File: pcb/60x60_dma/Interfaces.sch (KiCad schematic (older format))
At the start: 16 parts, among them J1 Conn_01x05, J10 Conn_01x01_Female, J11 Conn_01x01_Female, J12 Conn_01x01_Female, J13 Conn_01x01_Female, J14 Conn_01x02, J15 Conn_01x04, J2 Conn_01x05, J3 USB_OTG, J4 Conn_01x05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

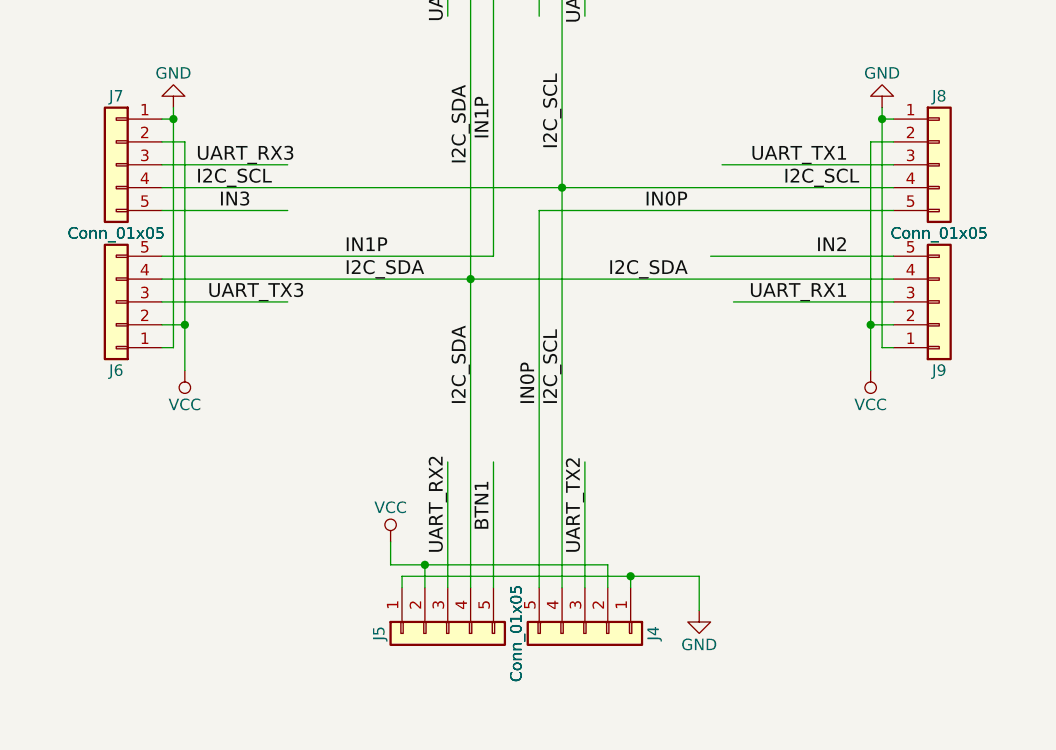
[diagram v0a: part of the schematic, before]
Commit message: - add 60x60_dma version
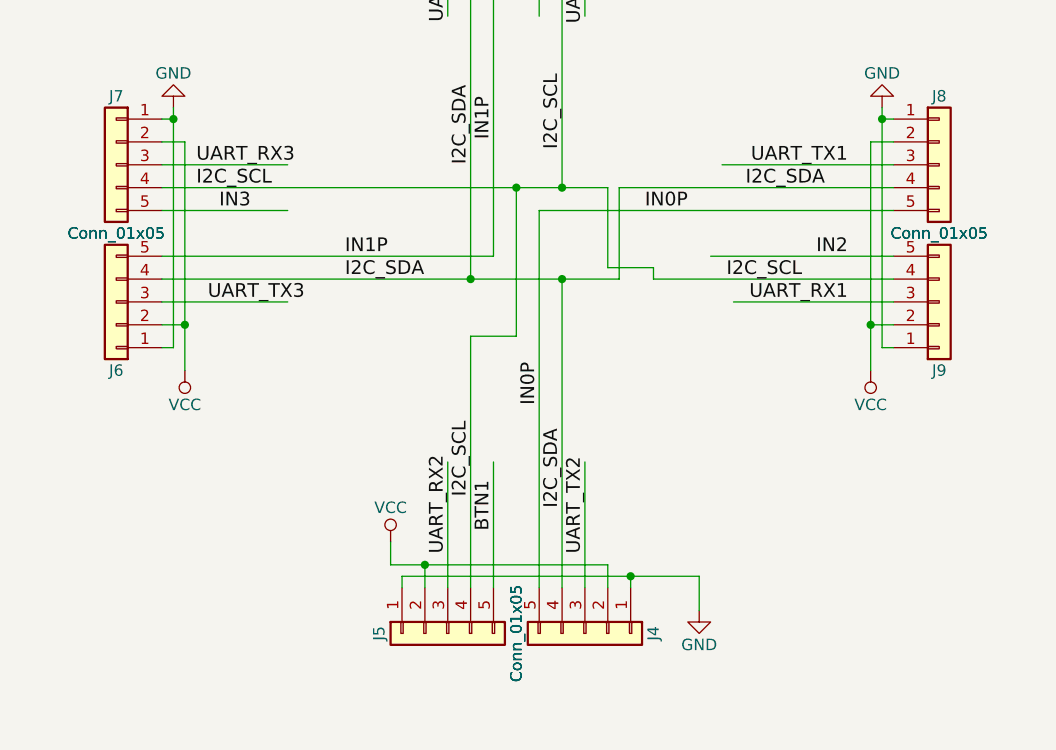
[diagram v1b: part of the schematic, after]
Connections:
- wire segments 96 -> 106
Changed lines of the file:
@@
 	-1   0    0    -1
 $EndComp
-Text Label 3950 4350 1    60   ~ 0
+Text Label 3550 4750 1    60   ~ 0
 I2C_SCL
 $Comp
@@
 	1    0    0    -1
 $EndComp
-Text Label 3550 4350 1    60   ~ 0
+Text Label 3950 4800 1    60   ~ 0
 I2C_SDA
 Text Label 4050 5000 1    60   ~ 0
@@
 Text Label 5200 3900 2    60   ~ 0
 UART_RX1
-Text Label 5250 3400 2    60   ~ 0
+Text Label 5000 3800 2    60   ~ 0
 I2C_SCL
 $Comp
@@
 	-1   0    0    1
 $EndComp
-Text Label 4500 3800 2    60   ~ 0
+Text Label 5100 3400 2    60   ~ 0
 I2C_SDA
 Text Label 2350 3300 0    60   ~ 0
@@
 	2200 3800 3550 3800
 Wire Wire Line
-	2200 3400 3950 3400
+	2200 3400 3750 3400
 Wire Wire Line
 	9450 3900 9850 3900
@@
 	9300 2300 9300 2350
 Wire Wire Line
-	3950 3400 3950 5150
-Wire Wire Line
-	3950 3400 5400 3400
-Wire Wire Line
-	3550 3800 3550 5150
-Wire Wire Line
-	3550 3800 5400 3800
+	5400 3400 4200 3400
+Wire Wire Line
+	4200 3400 4200 3800
+Wire Wire Line
+	4200 3800 3950 3800
+Wire Wire Line
+	3950 3400 4150 3400
+Wire Wire Line
+	4150 3400 4150 3750
+Wire Wire Line
+	4150 3750 4350 3750
+Wire Wire Line
+	4350 3750 4350 3800
+Wire Wire Line
+	4350 3800 5400 3800
+Wire Wire Line
+	3950 3800 3950 5150
+Connection ~ 3950 3800
+Wire Wire Line
+	3950 3800 3550 3800
+Wire Wire Line
+	3550 5150 3550 4050
+Wire Wire Line
+	3550 4050 3750 4050
+Wire Wire Line
+	3750 4050 3750 3400
+Connection ~ 3750 3400
+Wire Wire Line
+	3750 3400 3950 3400
 $EndSCHEMATC

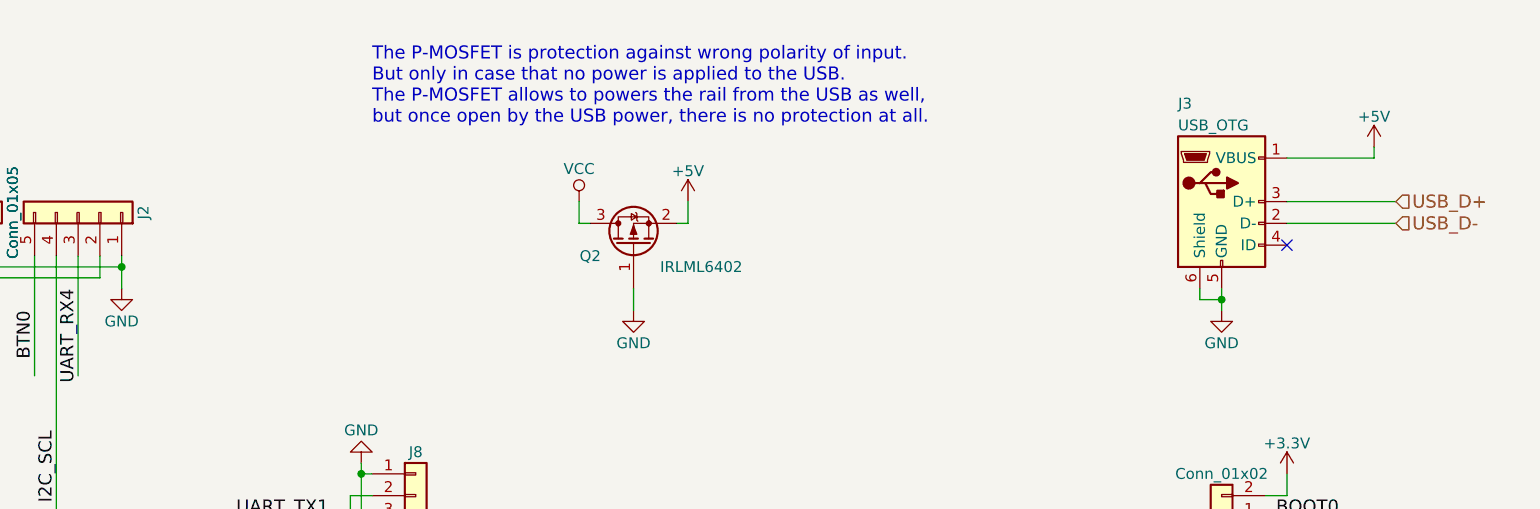
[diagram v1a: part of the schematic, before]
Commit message: - add some testpoints
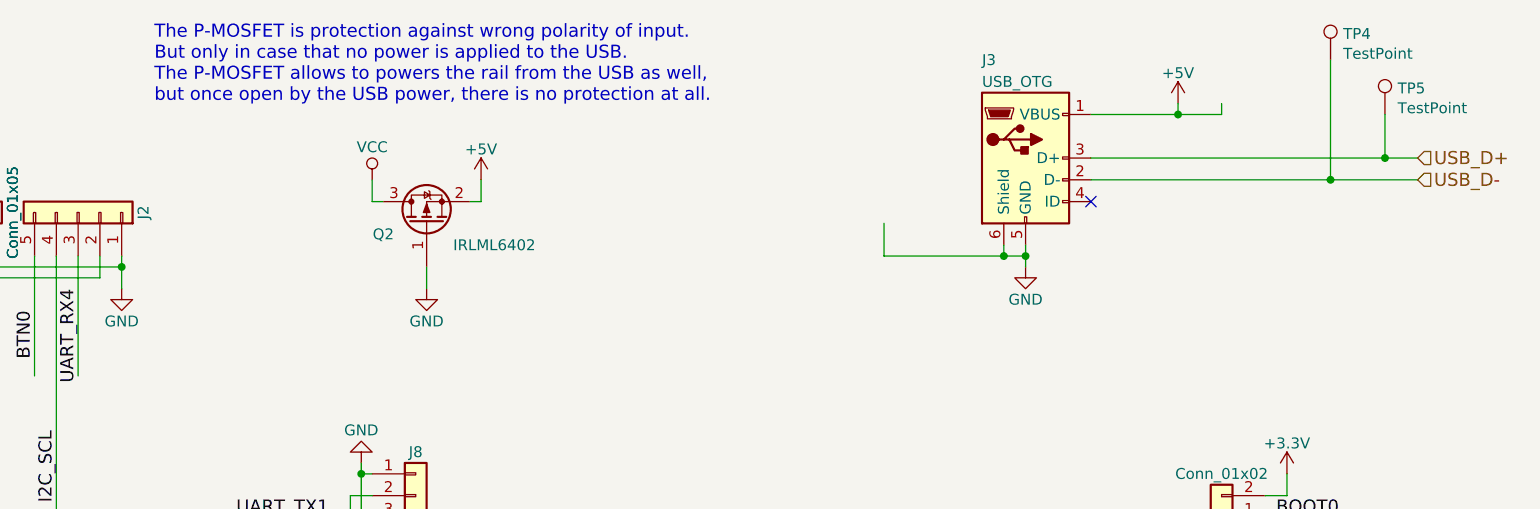
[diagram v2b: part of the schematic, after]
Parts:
- added TP4, TP5: TestPoint, symbol Connector:TestPoint
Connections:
- wire segments 106 -> 114
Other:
- moved on the sheet: J3, Q2
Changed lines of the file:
@@
 L bcl4v2-rescue:USB_OTG J3
 U 1 1 5BD73B46
-P 9300 1850
-F 0 "J3" H 9100 2300 50  0000 L CNN
-F 1 "USB_OTG" H 9100 2200 50  0000 L CNN
-F 2 "Connect:USB_Micro-B" H 9450 1800 50  0001 C CNN
-F 3 "" H 9450 1800 50  0001 C CNN
-	1    9300 1850
-	1    0    0    -1
-$EndComp
-NoConn ~ 9600 2050
+P 8400 1650
+F 0 "J3" H 8200 2100 50  0000 L CNN
+F 1 "USB_OTG" H 8200 2000 50  0000 L CNN
+F 2 "Connect:USB_Micro-B" H 8550 1600 50  0001 C CNN
+F 3 "" H 8550 1600 50  0001 C CNN
+	1    8400 1650
+	1    0    0    -1
+$EndComp
+NoConn ~ 8700 1850
 $Comp
 L bcl4v2-rescue:+5V #PWR039
 U 1 1 5BD73B57
-P 10000 1600
-F 0 "#PWR039" H 10000 1450 50  0001 C CNN
-F 1 "+5V" H 10000 1740 50  0000 C CNN
-F 2 "" H 10000 1600 50  0001 C CNN
-F 3 "" H 10000 1600 50  0001 C CNN
-	1    10000 1600
+P 9100 1400
+F 0 "#PWR039" H 9100 1250 50  0001 C CNN
+F 1 "+5V" H 9100 1540 50  0000 C CNN
+F 2 "" H 9100 1400 50  0001 C CNN
+F 3 "" H 9100 1400 50  0001 C CNN
+	1    9100 1400
 	1    0    0    -1
 $EndComp
@@
 L bcl4v2-rescue:GND #PWR042
 U 1 1 5BD73B89
-P 9300 2350
-F 0 "#PWR042" H 9300 2100 50  0001 C CNN
-F 1 "GND" H 9300 2200 50  0000 C CNN
-F 2 "" H 9300 2350 50  0001 C CNN
-F 3 "" H 9300 2350 50  0001 C CNN
-	1    9300 2350
+P 8400 2150
+F 0 "#PWR042" H 8400 1900 50  0001 C CNN
+F 1 "GND" H 8400 2000 50  0000 C CNN
+F 2 "" H 8400 2150 50  0001 C CNN
+F 3 "" H 8400 2150 50  0001 C CNN
+	1    8400 2150
 	1    0    0    -1
 $EndComp
@@
 Text HLabel 5400 6200 0    60   Input ~ 0
 I2C_SCL
-Text HLabel 10100 1950 2    60   Input ~ 0
+Text HLabel 10200 1750 2    60   Input ~ 0
 USB_D-
-Text HLabel 10100 1850 2    60   Input ~ 0
+Text HLabel 10200 1650 2    60   Input ~ 0
 USB_D+
 Text HLabel 3700 6150 0    60   Input ~ 0
@@
 L bcl4v2-rescue:+5V #PWR043
 U 1 1 5BDD7179
-P 6850 1850
-F 0 "#PWR043" H 6850 1700 50  0001 C CNN
-F 1 "+5V" H 6850 1990 50  0000 C CNN
-F 2 "" H 6850 1850 50  0001 C CNN
-F 3 "" H 6850 1850 50  0001 C CNN
-	1    6850 1850
+P 5900 1750
+F 0 "#PWR043" H 5900 1600 50  0001 C CNN
+F 1 "+5V" H 5900 1890 50  0000 C CNN
+F 2 "" H 5900 1750 50  0001 C CNN
+F 3 "" H 5900 1750 50  0001 C CNN
+	1    5900 1750
 	1    0    0    -1
 $EndComp
@@
 L bcl4v2-rescue:VCC #PWR044
 U 1 1 5BDD717F
-P 6350 1850
-F 0 "#PWR044" H 6350 1700 50  0001 C CNN
-F 1 "VCC" H 6350 2000 50  0000 C CNN
-F 2 "" H 6350 1850 50  0001 C CNN
-F 3 "" H 6350 1850 50  0001 C CNN
-	1    6350 1850
+P 5400 1750
+F 0 "#PWR044" H 5400 1600 50  0001 C CNN
+F 1 "VCC" H 5400 1900 50  0000 C CNN
+F 2 "" H 5400 1750 50  0001 C CNN
+F 3 "" H 5400 1750 50  0001 C CNN
+	1    5400 1750
 	1    0    0    -1
 $EndComp
@@
 L bcl4v2-rescue:Q_PMOS_GSD Q2
 U 1 1 5BDD7457
-P 6600 2050
-F 0 "Q2" V 6550 2200 50  0000 L CNN
-F 1 "IRLML6402" V 6500 1550 50  0000 L CNN
-F 2 "kicad_libraries_new:badger_SOT-23_handsolder" H 6800 2150 50  0001 C CNN
-F 3 "" H 6600 2050 50  0001 C CNN
-	1    6600 2050
+P 5650 1950
+F 0 "Q2" V 5600 2100 50  0000 L CNN
+F 1 "IRLML6402" V 5550 1450 50  0000 L CNN
+F 2 "kicad_libraries_new:badger_SOT-23_handsolder" H 5850 2050 50  0001 C CNN
+F 3 "" H 5650 1950 50  0001 C CNN
+	1    5650 1950
 	0    -1   -1   0
 $EndComp
@@
 L bcl4v2-rescue:GND #PWR045
 U 1 1 5BDD7A19
-P 6600 2350
-F 0 "#PWR045" H 6600 2100 50  0001 C CNN
-F 1 "GND" H 6600 2200 50  0000 C CNN
-F 2 "" H 6600 2350 50  0001 C CNN
-F 3 "" H 6600 2350 50  0001 C CNN
-	1    6600 2350
-	1    0    0    -1
-$EndComp
-Text Notes 5400 1500 0    60   ~ 0
+P 5650 2250
+F 0 "#PWR045" H 5650 2000 50  0001 C CNN
+F 1 "GND" H 5650 2100 50  0000 C CNN
+F 2 "" H 5650 2250 50  0001 C CNN
+F 3 "" H 5650 2250 50  0001 C CNN
+	1    5650 2250
+	1    0    0    -1
+$EndComp
+Text Notes 4400 1400 0    60   ~ 0
 The P-MOSFET is protection against wrong polarity of input.\nBut only in case that no power is applied to the USB.\nThe P-MOSFET allows to powers the rail from the USB as well,\nbut once open by the USB power, there is no protection at all.
 Text Label 1650 6850 0    60   ~ 0
@@
 	9450 3800 9850 3800
 Wire Wire Line
-	9200 2250 9200 2300
-Wire Wire Line
-	9200 2300 9300 2300
-Wire Wire Line
-	9300 2250 9300 2300
-Connection ~ 9300 2300
-Wire Wire Line
-	9600 1850 10100 1850
-Wire Wire Line
-	9600 1950 10100 1950
-Wire Wire Line
-	9600 1650 10000 1650
-Wire Wire Line
-	10000 1650 10000 1600
+	8300 2050 8300 2100
+Wire Wire Line
+	8300 2100 8400 2100
+Wire Wire Line
+	8400 2050 8400 2100
+Connection ~ 8400 2100
+Wire Wire Line
+	8700 1450 9100 1450
+Wire Wire Line
+	9100 1450 9100 1400
 Wire Wire Line
 	9500 3300 9850 3300
@@
 	9600 3200 9600 3100
 Wire Wire Line
-	6600 2250 6600 2350
-Wire Wire Line
-	6850 1950 6800 1950
-Wire Wire Line
-	6350 1950 6400 1950
-Wire Wire Line
-	6850 1850 6850 1950
-Wire Wire Line
-	6350 1850 6350 1950
+	5650 2150 5650 2250
+Wire Wire Line
+	5900 1850 5850 1850
+Wire Wire Line
+	5400 1850 5450 1850
+Wire Wire Line
+	5900 1750 5900 1850
+Wire Wire Line
+	5400 1750 5400 1850
 Wire Wire Line
 	1600 6100 2100 6100
@@
 	2300 4000 2300 3200
 Wire Wire Line
-	9300 2300 9300 2350
+	8400 2100 8400 2150
 Wire Wire Line
 	5400 3400 4200 3400
@@
 Wire Wire Line
 	3750 3400 3950 3400
+$Comp
+L Connector:TestPoint TP4
+U 1 1 5C7F78D4
+P 9800 1200
+F 0 "TP4" H 9858 1320 50  0000 L CNN
+F 1 "TestPoint" H 9858 1229 50  0000 L CNN
+F 2 "" H 10000 1200 50  0001 C CNN
+F 3 "~" H 10000 1200 50  0001 C CNN
+	1    9800 1200
+	1    0    0    -1
+$EndComp
+Wire Wire Line
+	8300 2100 7750 2100
+Wire Wire Line
+	7750 2100 7750 1950
+Connection ~ 8300 2100
+Wire Wire Line
+	9300 1400 9300 1450
+Wire Wire Line
+	9300 1450 9100 1450
+Connection ~ 9100 1450
+Wire Wire Line
+	8700 1650 10050 1650
+Wire Wire Line
+	8700 1750 9800 1750
+Wire Wire Line
+	9800 1200 9800 1750
+Connection ~ 9800 1750
+Wire Wire Line
+	9800 1750 10200 1750
+Wire Wire Line
+	10050 1450 10050 1650
+Connection ~ 10050 1650
+Wire Wire Line
+	10050 1650 10200 1650
+$Comp
+L Connector:TestPoint TP5
+U 1 1 5C7F782D
+P 10050 1450
+F 0 "TP5" H 10108 1570 50  0000 L CNN
+F 1 "TestPoint" H 10108 1479 50  0000 L CNN
+F 2 "" H 10250 1450 50  0001 C CNN
+F 3 "~" H 10250 1450 50  0001 C CNN
+	1    10050 1450
+	1    0    0    -1
+$EndComp
 $EndSCHEMATC

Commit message: - fix display connections, add testpoints
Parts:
- TP4, TP5: footprint (none) -> TestPoint:TestPoint_Pad_D1.0mm
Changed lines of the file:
@@
 F 0 "TP4" H 9858 1320 50  0000 L CNN
 F 1 "TestPoint" H 9858 1229 50  0000 L CNN
-F 2 "" H 10000 1200 50  0001 C CNN
+F 2 "TestPoint:TestPoint_Pad_D1.0mm" H 10000 1200 50  0001 C CNN
 F 3 "~" H 10000 1200 50  0001 C CNN
 	1    9800 1200
@@
 F 0 "TP5" H 10108 1570 50  0000 L CNN
 F 1 "TestPoint" H 10108 1479 50  0000 L CNN
-F 2 "" H 10250 1450 50  0001 C CNN
+F 2 "TestPoint:TestPoint_Pad_D1.0mm" H 10250 1450 50  0001 C CNN
 F 3 "~" H 10250 1450 50  0001 C CNN
 	1    10050 1450

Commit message: - clense the schematics
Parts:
- removed Q2: IRLML6402, kicad_libraries_new:badger_SOT-23_handsolder, symbol bcl4v2-rescue:Q_PMOS_GSD
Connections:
- net labels added: D+, D-
- wire segments 114 -> 113
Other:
- note removed: "The P-MOSFET is protection against wrong polarity of input.\nBut only in case that no power is applied to the USB.\nThe P-MOSFET allows to powers the rail from the USB as well,\nbut once open by the USB power, there is no protection at all."
- moved on the sheet: J1, J2, J3, J4, J5, J6, J7, J8, J9, TP4, TP5
